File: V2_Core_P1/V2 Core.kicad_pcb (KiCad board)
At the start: 4 copper layers, 90 x 110 mm, 340 parts, among them J1 USB_B, J10 Conn_01x02, J11 Conn_01x02, J12 Conn_01x02, J15 Conn_01x02, J16 Conn_01x02, J2 USB_A, J21 Conn_01x02, J22 Conn_01x02, J23 Conn_01x02, J24 Conn_01x03, J25 Conn_01x03, J26 Conn_01x03, J27 Conn_01x03, J28 Conn_01x03, J29 Conn_01x03, J3 Micro_SD_Card_Det, J30 Conn_01x03_Male, J32 Conn_02x05_Odd_Even, J33 Conn_02x05_Odd_Even, J34 Conn_02x05_Odd_Even, J35 Conn_02x05_Odd_Even, J36 Conn_02x05_Odd_Even, J37 Conn_02x05_Odd_Even, J38 Conn_02x05_Odd_Even, J39 Conn_02x05_Odd_Even, J4 RJ45_Hanrun_HR911105A, J40 Conn_02x05_Odd_Even, J41 Conn_ARM_JTAG_SWD_10, J42 Conn_01x02, J43 Conn_01x02, J44 Conn_01x02, J45 Conn_01x02, J5 Conn_02x20_Odd_Even, J6 Conn_01x03, J7 Conn_01x02, J8 Conn_01x02, J9 Conn_01x02, Q1 2N7002, Q2 2N7002, Q23 CJ2301 S1, Q24 CJ2301 S1, Q26 2N7002, Q27 MBT3906DW1, Q28 SQ3493EV, Q29 MBT3906DW1, Q3 2N7002, Q30 SQ3493EV, Q31 MBT3906DW1, Q32 SQ3493EV, Q4 WSD30L40DN, Q5 WSD3066DN33, Q6 2N7002, Q8 WSD3066DN33, SW1 SW_Push, SW2 TS-1185EC-C-D-B, U1 LAN8720A, U10 TPD4E1U06DCKR, U11 TPD4E1U06DCKR, U12 LMV324, U13 TPD4E1U06DCKR, U14 TPD4E1U06DCKR, U15 74LCX07, U16 MT9700, U17 TPD4E1U06DCKR, U18 MT9700, U19 MT9700, U2 STM32H745XIHx, U20 MT9700, U21 TPS5430DDA, U22 MT3410L, U23 AP22814AW5, U24 LMV331, U25 BD4722G, U4 AT25SF081-SSHF-X, U8 TPD4E1U06DCKR, U9 74HCT541, Y1 Crystal_GND24, Y2 Crystal, Y3 Crystal_GND24

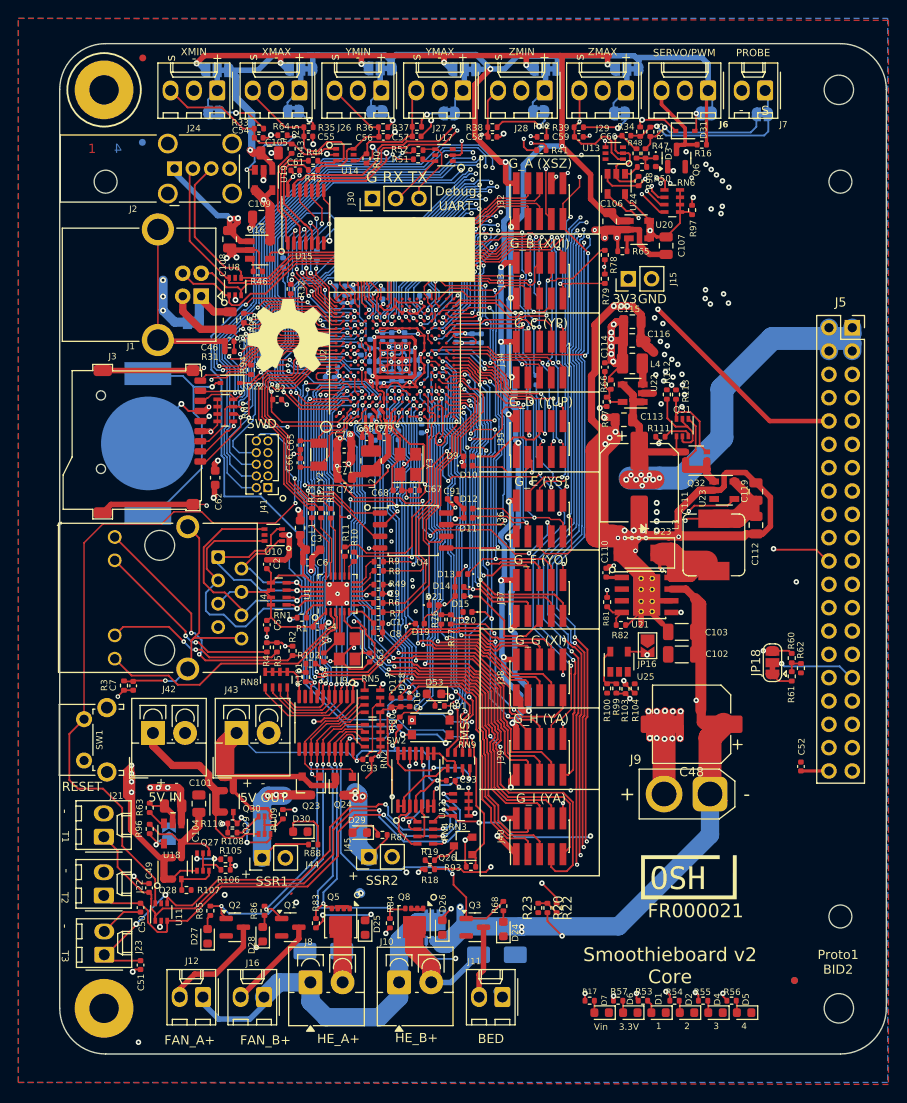
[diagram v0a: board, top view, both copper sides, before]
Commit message: Fix servo/pwm miswire to probe jumper
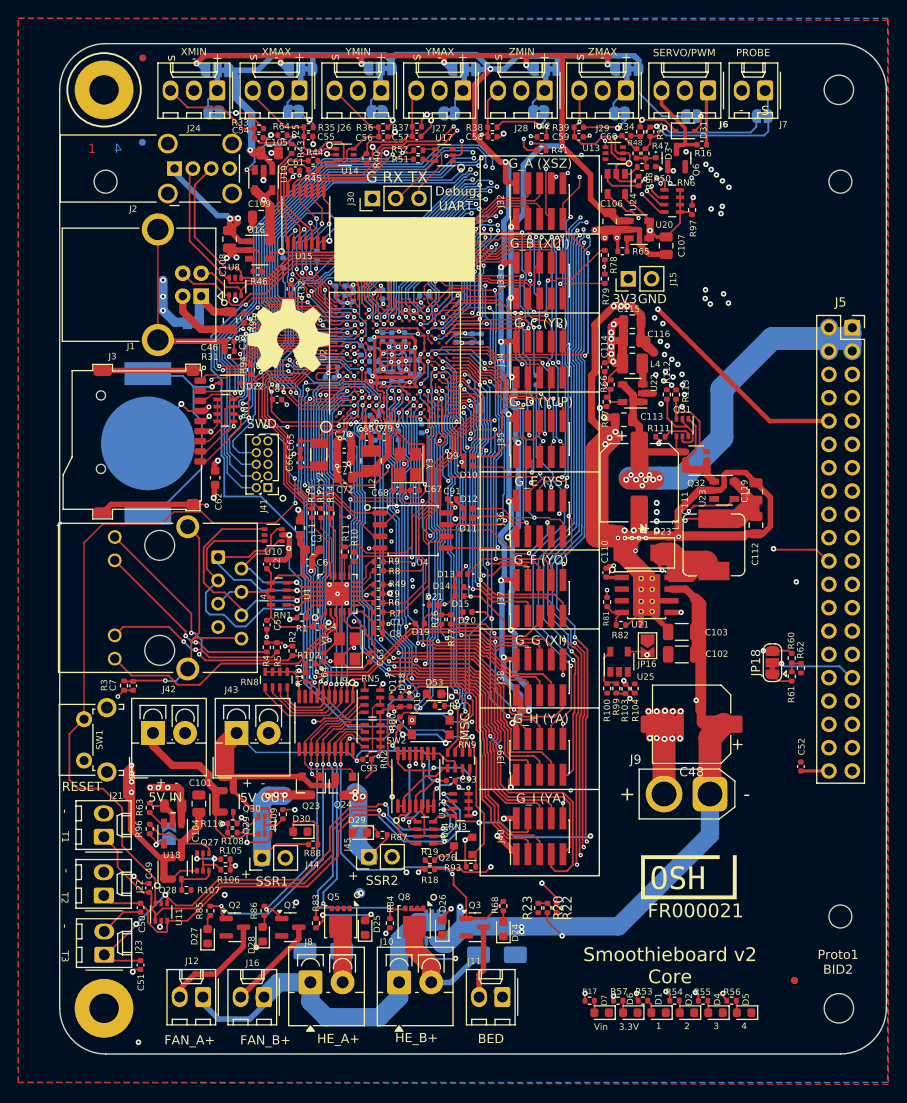
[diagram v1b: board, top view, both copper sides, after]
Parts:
- moved JP7 1.63 mm to (168.8, 45.9), turned to 0 degrees
- moved JP8 0.20 mm to (176.5, 45.9)
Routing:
- net /5V_LIMIT: track 187.1 -> 179.5 mm
- net /5V_IN: track 99.1 -> 96.7 mm
- net GND: track 544.7 -> 543.2 mm
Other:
- board text added: "Keep hole in paste layer"
